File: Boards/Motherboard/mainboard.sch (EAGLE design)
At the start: 15 parts, among them IC1 7805TV

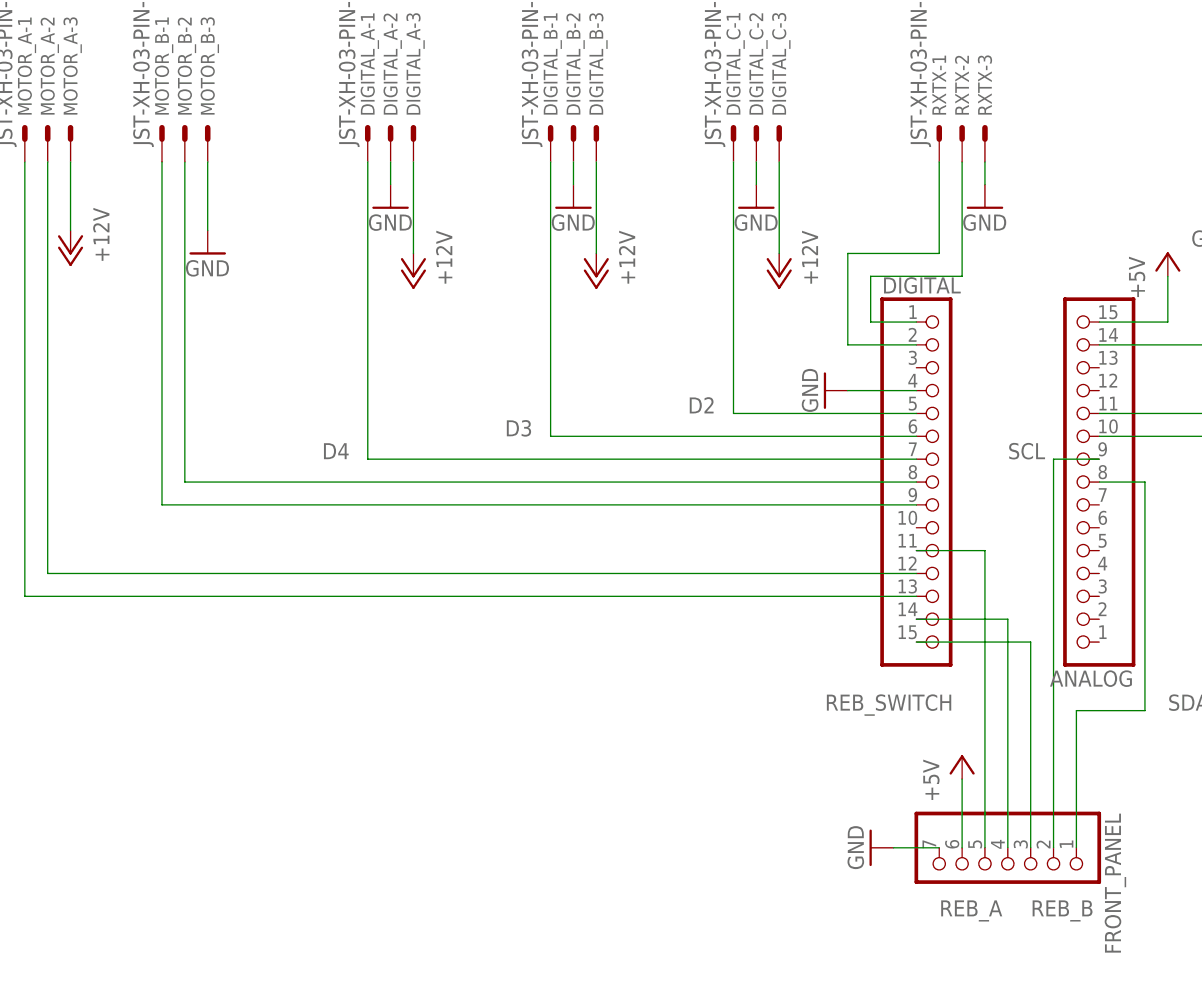
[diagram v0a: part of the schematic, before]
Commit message: * Changed the rotary encoder code, to match that of the following source:    - https://www.instructables.com/Tutorial-of-Rotary-Encoder-With-Arduino/ * Changed boards and schematic, so that interrupt pins are correct
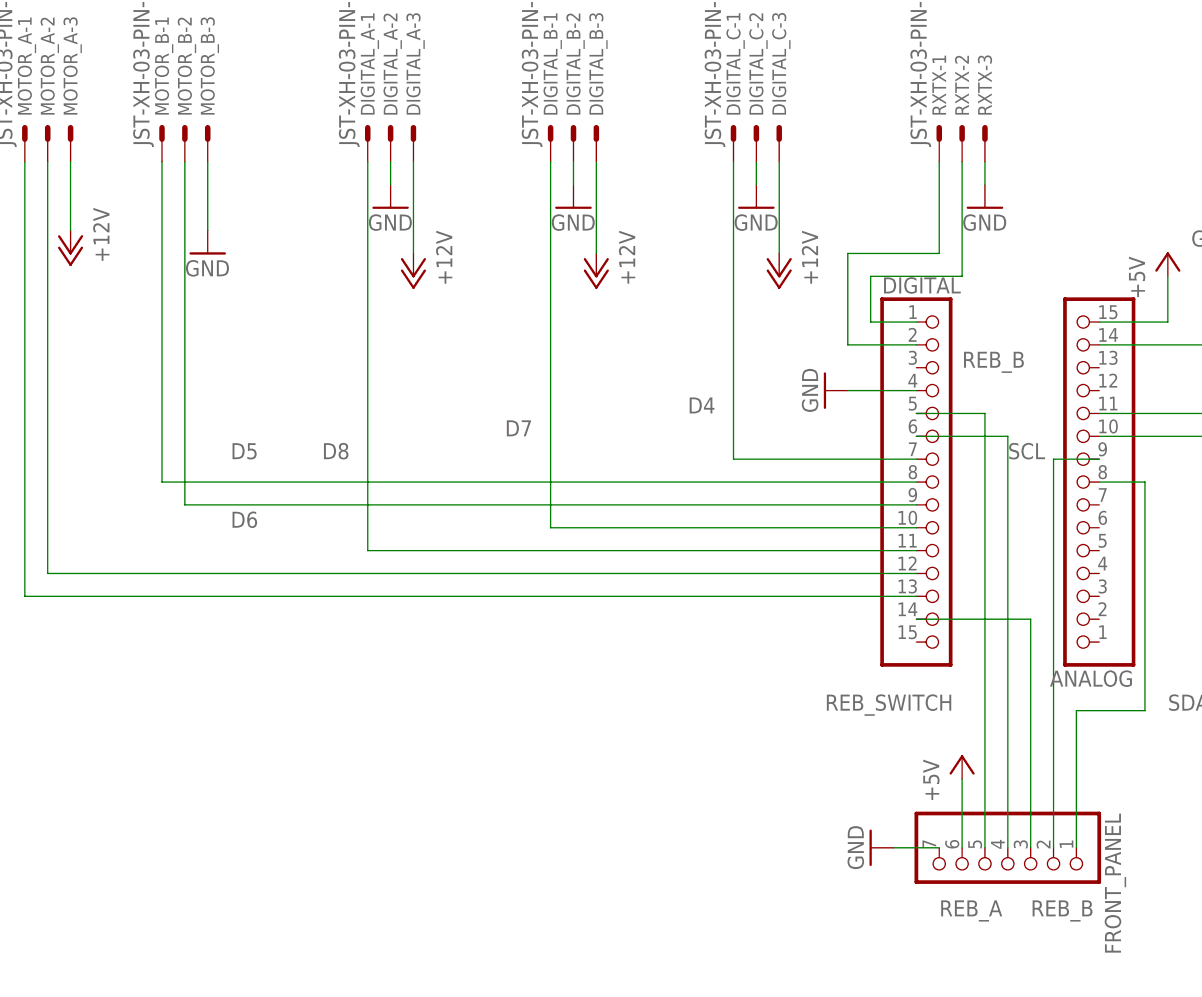
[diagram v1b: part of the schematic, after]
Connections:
- removed net D2: DIGITAL.5, DIGITAL_C-1.S
- removed net D3: DIGITAL.6, DIGITAL_B-1.S
- new net D7: DIGITAL.10, DIGITAL_B-1.S
- new net D8: DIGITAL.11, DIGITAL_A-1.S
- net D4: now also DIGITAL_C-1.S; no longer DIGITAL_A-1.S
- net D5: now also MOTOR_B-1.S; no longer MOTOR_B-2.S
- net D6: now also MOTOR_B-2.S; no longer MOTOR_B-1.S
- net REB_A: now also FRONT_PANEL.3; no longer FRONT_PANEL.4
- net REB_B: now also DIGITAL.5, FRONT_PANEL.5; no longer DIGITAL.15, FRONT_PANEL.3
- net REB_SWITCH: now also DIGITAL.6, FRONT_PANEL.4; no longer DIGITAL.11, FRONT_PANEL.5

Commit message: * Made some minor changes on the motherboard, so that the +5v rail is connected to +5v on the arduino instead of vin
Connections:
- net +5V: now also ANALOG.12; no longer ANALOG.15
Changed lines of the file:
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@@
 <attribute name="VALUE" x="20.32" y="132.08" size="1.778" layer="96" rot="R180"/>
 </instance>
-<instance part="P+5" gate="1" x="55.88" y="78.74" smashed="yes">
-<attribute name="VALUE" x="53.34" y="73.66" size="1.778" layer="96" rot="R90"/>
+<instance part="P+5" gate="1" x="63.5" y="63.5" smashed="yes" rot="R270">
+<attribute name="VALUE" x="58.42" y="66.04" size="1.778" layer="96"/>
 </instance>
 <instance part="GND3" gate="1" x="63.5" y="78.74" smashed="yes" rot="R180">
@@
 </segment>
 <segment>
-<pinref part="ANALOG" gate="A" pin="15"/>
-<wire x1="48.26" y1="71.12" x2="55.88" y2="71.12" width="0.1524" layer="91"/>
-<pinref part="P+5" gate="1" pin="+5V"/>
-<wire x1="55.88" y1="71.12" x2="55.88" y2="76.2" width="0.1524" layer="91"/>
-</segment>
-<segment>
 <pinref part="P+2" gate="1" pin="+5V"/>
 <pinref part="FRONT_PANEL" gate="A" pin="6"/>
 <wire x1="33.02" y1="20.32" x2="33.02" y2="12.7" width="0.1524" layer="91"/>
 </segment>
+<segment>
+<pinref part="P+5" gate="1" pin="+5V"/>
+<pinref part="ANALOG" gate="A" pin="12"/>
+<wire x1="60.96" y1="63.5" x2="48.26" y2="63.5" width="0.1524" layer="91"/>
+</segment>
 </net>

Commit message: * Optimised the motherboard a little
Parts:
- removed FRONT_PANEL: (no value), pinhead:PINHD-1X7
- added FRONT_PANEL_DATA: JST-XH-05-PIN-LONG-PAD, Rembrandt Electronics - JST XH Connectors v1-0:JST-XH-05-PIN-LONG-PAD
- added FRONT_PANEL_PWR: JST-XH-02-PIN-LONG-PAD, Rembrandt Electronics - JST XH Connectors v1-0:JST-XH-02-PIN-LONG-PAD
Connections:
- net +5V: now also FRONT_PANEL_PWR-1.S; no longer FRONT_PANEL.6
- net GND: now also FRONT_PANEL_PWR-2.S; no longer FRONT_PANEL.7
- net REB_A: now also FRONT_PANEL_DATA-3.S; no longer FRONT_PANEL.3
- net REB_B: now also FRONT_PANEL_DATA-5.S; no longer FRONT_PANEL.5
- net REB_SWITCH: now also FRONT_PANEL_DATA-4.S; no longer FRONT_PANEL.4
- net SCL: now also FRONT_PANEL_DATA-2.S; no longer FRONT_PANEL.2
- net SDA: now also FRONT_PANEL_DATA-1.S; no longer FRONT_PANEL.1
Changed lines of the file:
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@@
 <part name="ANALOG_A" library="Rembrandt Electronics - JST XH Connectors v1-0" deviceset="JST-XH-03-PIN" device="-LONG-PAD"/>
 <part name="ANALOG_B" library="Rembrandt Electronics - JST XH Connectors v1-0" deviceset="JST-XH-03-PIN" device="-LONG-PAD"/>
-<part name="FRONT_PANEL" library="pinhead" library_urn="urn:adsk.eagle:library:325" deviceset="PINHD-1X7" device="" package3d_urn="urn:adsk.eagle:package:22477/2"/>
 <part name="GND6" library="supply1" library_urn="urn:adsk.eagle:library:371" deviceset="GND" device=""/>
 <part name="P+2" library="supply1" library_urn="urn:adsk.eagle:library:371" deviceset="+5V" device=""/>
@@
 <part name="C3" library="SparkFun-Capacitors" library_urn="urn:adsk.eagle:library:510" deviceset="1000UF" device="-RADIAL-5MM-25V-20%" package3d_urn="urn:adsk.eagle:package:37412/1" value="1mF"/>
 <part name="C4" library="SparkFun-Capacitors" library_urn="urn:adsk.eagle:library:510" deviceset="1000UF" device="-RADIAL-5MM-25V-20%" package3d_urn="urn:adsk.eagle:package:37412/1" value="1mF"/>
+<part name="FRONT_PANEL_DATA" library="Rembrandt Electronics - JST XH Connectors v1-0" deviceset="JST-XH-05-PIN" device="-LONG-PAD"/>
+<part name="FRONT_PANEL_PWR" library="Rembrandt Electronics - JST XH Connectors v1-0" deviceset="JST-XH-02-PIN" device="-LONG-PAD"/>
 </parts>
 <sheets>
@@
 <attribute name="NAME" x="99.822" y="93.98" size="1.524" layer="95" rot="R90"/>
 </instance>
-<instance part="FRONT_PANEL" gate="A" x="38.1" y="10.16" smashed="yes" rot="R270">
-<attribute name="NAME" x="48.895" y="16.51" size="1.778" layer="95" rot="R270"/>
-<attribute name="VALUE" x="25.4" y="16.51" size="1.778" layer="96" rot="R270"/>
-</instance>
-<instance part="GND6" gate="1" x="22.86" y="12.7" smashed="yes" rot="R270">
-<attribute name="VALUE" x="20.32" y="15.24" size="1.778" layer="96" rot="R270"/>
-</instance>
-<instance part="P+2" gate="1" x="33.02" y="22.86" smashed="yes">
-<attribute name="VALUE" x="30.48" y="17.78" size="1.778" layer="96" rot="R90"/>
+<instance part="GND6" gate="1" x="20.32" y="17.78" smashed="yes" rot="R270">
+<attribute name="VALUE" x="17.78" y="20.32" size="1.778" layer="96" rot="R270"/>
+</instance>
+<instance part="P+2" gate="1" x="33.02" y="17.78" smashed="yes" rot="R270">
+<attribute name="VALUE" x="27.94" y="20.32" size="1.778" layer="96"/>
 </instance>
 <instance part="GND7" gate="1" x="17.78" y="63.5" smashed="yes" rot="R270">
@@
 <attribute name="NAME" x="52.324" y="146.685" size="1.778" layer="95" font="vector" rot="R180"/>
 <attribute name="VALUE" x="52.324" y="151.511" size="1.778" layer="96" font="vector" rot="R180"/>
+</instance>
+<instance part="FRONT_PANEL_DATA" gate="-1" x="45.72" y="10.16" smashed="yes" rot="R270">
+<attribute name="NAME" x="44.958" y="7.62" size="1.524" layer="95" rot="R270"/>
+<attribute name="VALUE" x="47.117" y="10.922" size="1.778" layer="96" rot="R270"/>
+</instance>
+<instance part="FRONT_PANEL_DATA" gate="-2" x="43.18" y="10.16" smashed="yes" rot="R270">
+<attribute name="NAME" x="42.418" y="7.62" size="1.524" layer="95" rot="R270"/>
+</instance>
+<instance part="FRONT_PANEL_DATA" gate="-3" x="40.64" y="10.16" smashed="yes" rot="R270">
+<attribute name="NAME" x="39.878" y="7.62" size="1.524" layer="95" rot="R270"/>
+</instance>
+<instance part="FRONT_PANEL_DATA" gate="-4" x="38.1" y="10.16" smashed="yes" rot="R270">
+<attribute name="NAME" x="37.338" y="7.62" size="1.524" layer="95" rot="R270"/>
+</instance>
+<instance part="FRONT_PANEL_DATA" gate="-5" x="35.56" y="10.16" smashed="yes" rot="R270">
+<attribute name="NAME" x="34.798" y="7.62" size="1.524" layer="95" rot="R270"/>
+</instance>
+<instance part="FRONT_PANEL_PWR" gate="-2" x="25.4" y="10.16" smashed="yes" rot="R270">
+<attribute name="NAME" x="24.638" y="7.62" size="1.524" layer="95" rot="R270"/>
+</instance>
+<instance part="FRONT_PANEL_PWR" gate="-1" x="27.94" y="10.16" smashed="yes" rot="R270">
+<attribute name="NAME" x="27.178" y="7.62" size="1.524" layer="95" rot="R270"/>
+<attribute name="VALUE" x="29.337" y="10.922" size="1.778" layer="96" rot="R270"/>
 </instance>
 </instances>
@@
 </segment>
 <segment>
-<pinref part="FRONT_PANEL" gate="A" pin="7"/>
-<pinref part="GND6" gate="1" pin="GND"/>
-<wire x1="30.48" y1="12.7" x2="25.4" y2="12.7" width="0.1524" layer="91"/>
-</segment>
-<segment>
 <pinref part="PWR" gate="-1" pin="S"/>
 <pinref part="GND12" gate="1" pin="GND"/>
@@
 <wire x1="53.34" y1="154.94" x2="53.34" y2="152.4" width="0.1524" layer="91"/>
 <pinref part="C4" gate="G$1" pin="-"/>
+</segment>
+<segment>
+<pinref part="GND6" gate="1" pin="GND"/>
+<pinref part="FRONT_PANEL_PWR" gate="-2" pin="S"/>
+<wire x1="22.86" y1="17.78" x2="25.4" y2="17.78" width="0.1524" layer="91"/>
+<wire x1="25.4" y1="17.78" x2="25.4" y2="12.7" width="0.1524" layer="91"/>
 </segment>
 </net>
@@
 </segment>
 <segment>
-<pinref part="P+2" gate="1" pin="+5V"/>
-<pinref part="FRONT_PANEL" gate="A" pin="6"/>
-<wire x1="33.02" y1="20.32" x2="33.02" y2="12.7" width="0.1524" layer="91"/>
-</segment>
-<segment>
 <pinref part="P+5" gate="1" pin="+5V"/>
 <pinref part="ANALOG" gate="A" pin="12"/>
 <wire x1="60.96" y1="63.5" x2="48.26" y2="63.5" width="0.1524" layer="91"/>
+</segment>
+<segment>
+<pinref part="FRONT_PANEL_PWR" gate="-1" pin="S"/>
+<pinref part="P+2" gate="1" pin="+5V"/>
+<wire x1="27.94" y1="12.7" x2="27.94" y2="17.78" width="0.1524" layer="91"/>
+<wire x1="27.94" y1="17.78" x2="30.48" y2="17.78" width="0.1524" layer="91"/>
 </segment>
 </net>
@@
 <pinref part="DIGITAL" gate="A" pin="14"/>
 <wire x1="40.64" y1="38.1" x2="27.94" y2="38.1" width="0.1524" layer="91"/>
-<label x="30.48" y="5.08" size="1.778" layer="95"/>
-<pinref part="FRONT_PANEL" gate="A" pin="3"/>
+<label x="40.64" y="38.1" size="1.778" layer="95" rot="R90"/>
 <wire x1="40.64" y1="12.7" x2="40.64" y2="38.1" width="0.1524" layer="91"/>
+<pinref part="FRONT_PANEL_DATA" gate="-3" pin="S"/>
 </segment>
 </net>
@@
 <wire x1="48.26" y1="53.34" x2="53.34" y2="53.34" width="0.1524" layer="91"/>
 <wire x1="53.34" y1="53.34" x2="53.34" y2="27.94" width="0.1524" layer="91"/>
-<pinref part="FRONT_PANEL" gate="A" pin="1"/>
 <wire x1="45.72" y1="12.7" x2="45.72" y2="27.94" width="0.1524" layer="91"/>
 <wire x1="45.72" y1="27.94" x2="53.34" y2="27.94" width="0.1524" layer="91"/>
 <label x="55.88" y="27.94" size="1.778" layer="95"/>
+<pinref part="FRONT_PANEL_DATA" gate="-1" pin="S"/>
 </segment>
 </net>
@@
 <segment>
 <pinref part="ANALOG" gate="A" pin="9"/>
-<pinref part="FRONT_PANEL" gate="A" pin="2"/>
 <wire x1="48.26" y1="55.88" x2="43.18" y2="55.88" width="0.1524" layer="91"/>
 <wire x1="43.18" y1="55.88" x2="43.18" y2="12.7" width="0.1524" layer="91"/>
-<label x="38.1" y="55.88" size="1.778" layer="95"/>
+<label x="43.18" y="55.88" size="1.778" layer="95" rot="R90"/>
+<pinref part="FRONT_PANEL_DATA" gate="-2" pin="S"/>
 </segment>
 </net>
 <net name="REB_SWITCH" class="0">
 <segment>
-<label x="17.78" y="27.94" size="1.778" layer="95"/>
+<label x="38.1" y="58.42" size="1.778" layer="95" rot="R90"/>
 <pinref part="DIGITAL" gate="A" pin="6"/>
 <wire x1="27.94" y1="58.42" x2="38.1" y2="58.42" width="0.1524" layer="91"/>
-<pinref part="FRONT_PANEL" gate="A" pin="4"/>
 <wire x1="38.1" y1="58.42" x2="38.1" y2="12.7" width="0.1524" layer="91"/>
+<pinref part="FRONT_PANEL_DATA" gate="-4" pin="S"/>
 </segment>
 </net>
 <net name="REB_B" class="0">
 <segment>
-<label x="40.64" y="5.08" size="1.778" layer="95"/>
+<label x="35.56" y="60.96" size="1.778" layer="95" rot="R90"/>
 <pinref part="DIGITAL" gate="A" pin="5"/>
 <wire x1="27.94" y1="60.96" x2="35.56" y2="60.96" width="0.1524" layer="91"/>
-<label x="33.02" y="66.04" size="1.778" layer="95"/>
-<pinref part="FRONT_PANEL" gate="A" pin="5"/>
 <wire x1="35.56" y1="60.96" x2="35.56" y2="12.7" width="0.1524" layer="91"/>
-</segment>
-</net>
+<pinref part="FRONT_PANEL_DATA" gate="-5" pin="S"/>
+</segment>
+</net>
